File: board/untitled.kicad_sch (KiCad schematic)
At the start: 52 parts, among them J5 I2C_3V3, Q10 BC548, Q11 BC548, Q12 BC548, Q13 BC548, Q14 BC548, Q15 BC548, Q16 BC548, Q17 BC548, Q7 BC548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

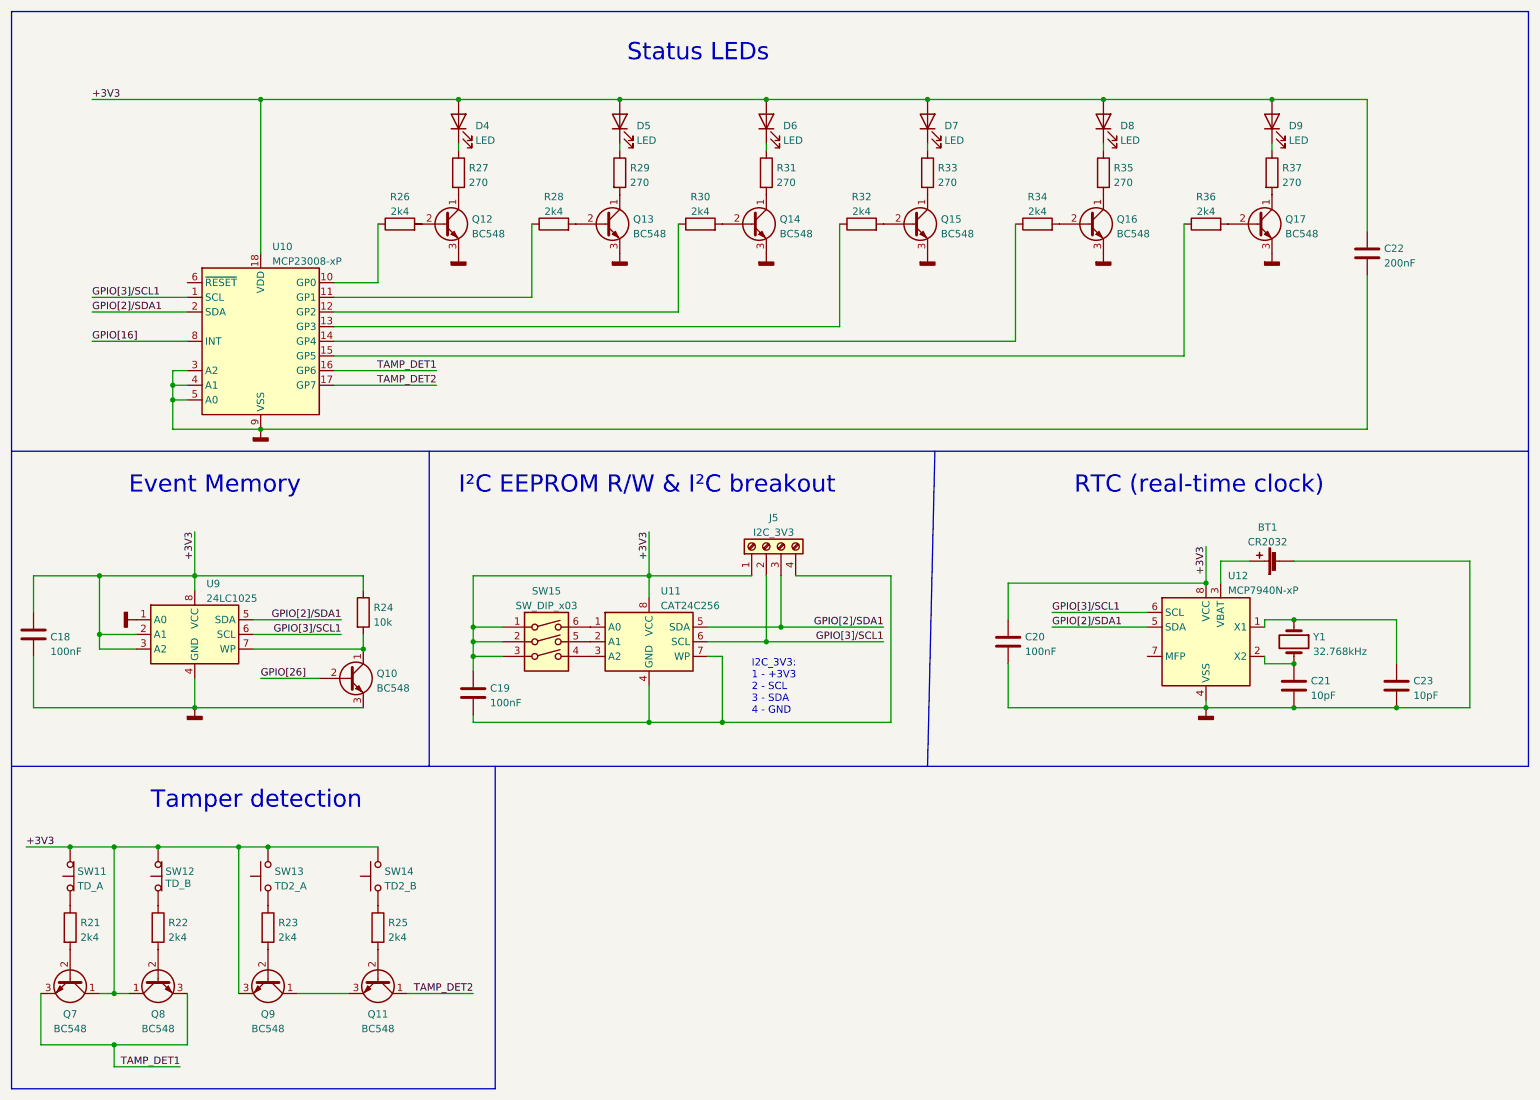
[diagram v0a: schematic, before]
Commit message: Fix typos and label names.
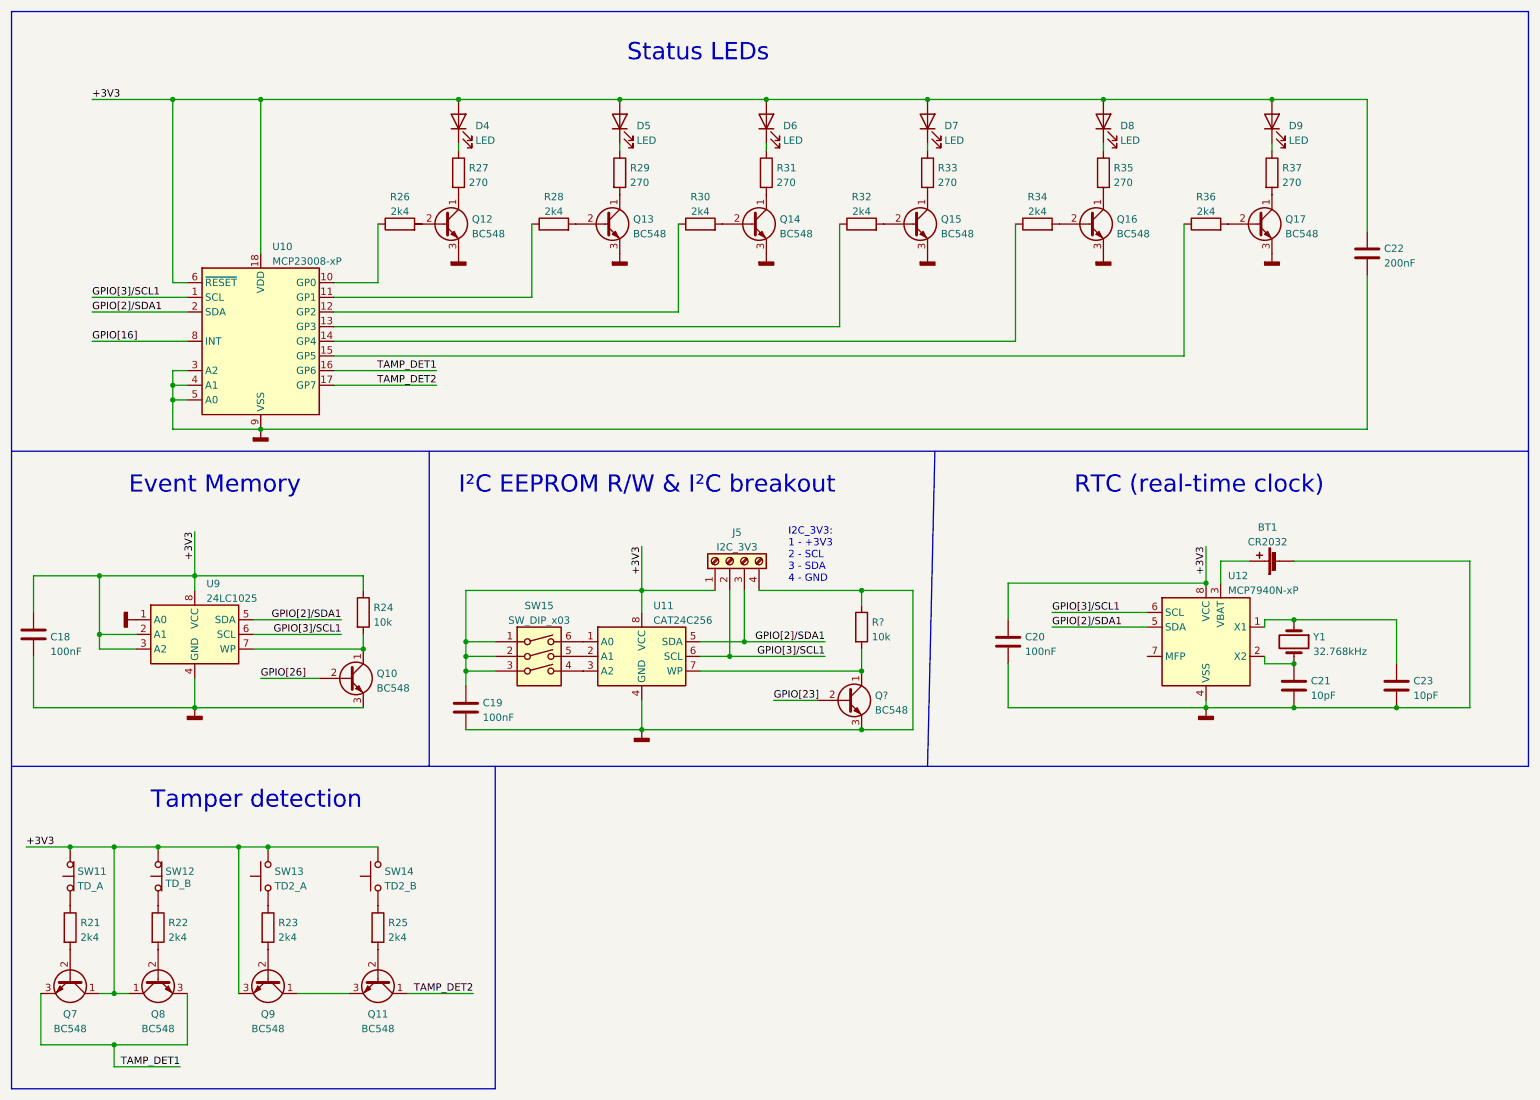
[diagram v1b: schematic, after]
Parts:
- added Q?: BC548, Package_TO_SOT_THT:TO-92_Inline, symbol Transistor_BJT:BC548
- added R?: 10k, symbol Device:R
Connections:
- net +3V3: now also U10.6 (~{RESET})
- net GNDD: now also C19.2, J5.4 (Pin_4), U11.4 (GND), Q?.3 (E), R?.1
- new net: Q?.1 (C), R?.2, U11.7 (WP)
- new net GPIO[23]: Q?.2 (B)
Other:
- moved on the sheet: C19, J5, SW15, U11

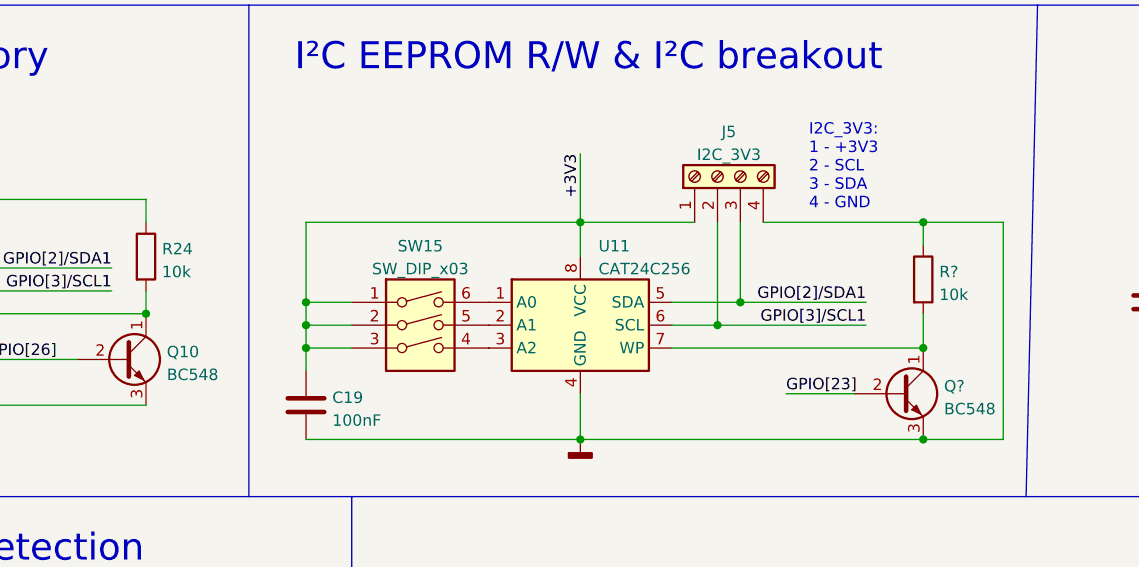
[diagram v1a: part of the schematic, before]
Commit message: Change EEPROM write protection Ppull-up resistor value to 1k.
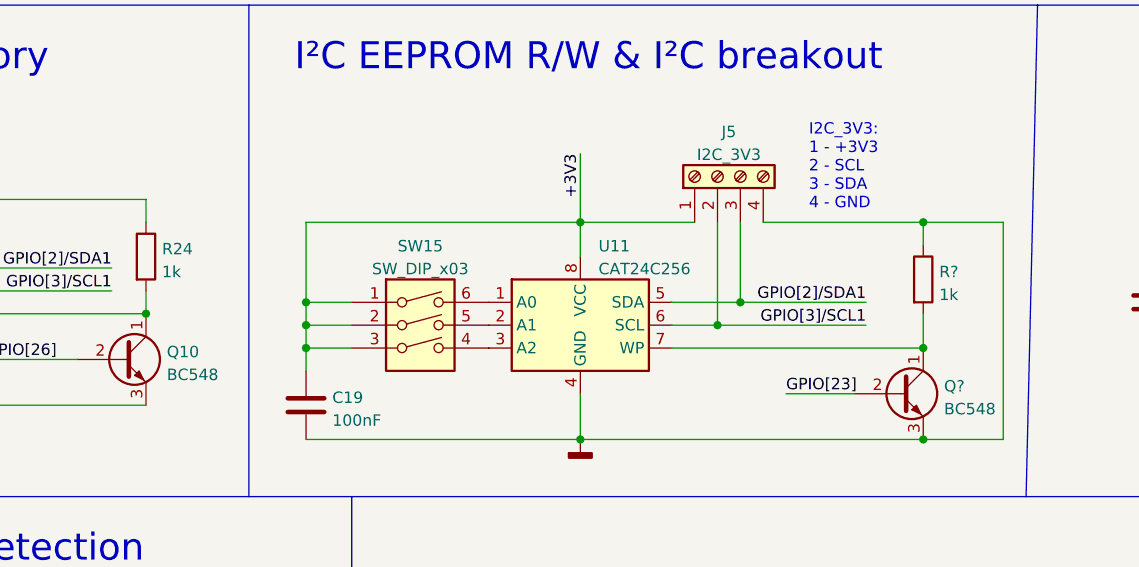
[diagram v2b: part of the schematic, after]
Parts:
- R24, R?: value 10k -> 1k
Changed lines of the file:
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@@
       (effects (font (size 1.27 1.27)) (justify left))
     )
-    (property "Value" "10k" (id 1) (at 76.708 118.5422 0)
+    (property "Value" "1k" (id 1) (at 76.708 118.5422 0)
       (effects (font (size 1.27 1.27)) (justify left))
     )
@@
       (effects (font (size 1.27 1.27)) (justify left))
     )
-    (property "Value" "10k" (id 1) (at 163.068 121.0822 0)
-      (effects (font (size 1.27 1.27)) (justify left))
-    )
+    (property "Value" "1k" (id 1) (at 163.068 121.0822 0)
+      (effects (font (size 1.27 1.27)) (justify left))
+    )
